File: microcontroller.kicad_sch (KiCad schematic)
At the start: 3 parts, among them J6 JTAG_connector, SW1 SW_Push, U1 STM32G473CBTx

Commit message: Finished schematic and first layout
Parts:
- removed U1: STM32G473CBTx, Package_QFP:LQFP-48_7x7mm_P0.5mm, symbol MCU_ST_STM32G4:STM32G473CBTx
- added C20: 4,7uF, Capacitor_SMD:C_0805_2012Metric, symbol Device:C
- added C21, C22, C23, C24: 100nF, Capacitor_SMD:C_0805_2012Metric, symbol Device:C
- added C25: 1uF, Capacitor_SMD:C_0805_2012Metric, symbol Device:C
- added C26: 10nF, Capacitor_SMD:C_0805_2012Metric, symbol Device:C
- added C28: 0.1uF, Capacitor_SMD:C_0805_2012Metric, symbol Device:C
- added R20: 0, Resistor_SMD:R_0805_2012Metric, symbol Device:R
- added R28: 10k, Resistor_SMD:R_0805_2012Metric, symbol Device:R
- added R29: 1k, Resistor_SMD:R_0805_2012Metric, symbol Device:R
- added U4: STM32F103RGTx, Package_QFP:LQFP-64_10x10mm_P0.5mm, symbol MCU_ST_STM32F1:STM32F103RGTx
- added X1: 831066657, footprints:831066657, symbol my_library:831066657
- J6: footprint (none) -> footprints:627010021621
- SW1: footprint (none) -> footprints:SWT0310
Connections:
- net at SW1.1: now also R29.2
- net +3.3V: now reaches J6.1 (VTref)
- net +3.3V: now also C20.1, C21.1, C22.1, C23.1, C24.1, C25.1, C26.1, R28.1, U4.1 (VBAT), U4.13 (VDDA), U4.19 (VDD), U4.32 (VDD), U4.48 (VDD), U4.64 (VDD), X1.4 (VCC)
- net reset: now reaches J6.10 (~{RESET})
- net reset: now also U4.7 (NRST)
- net swdio: now reaches J6.2 (SWDIO/TMS)
- net swdio: now also U4.46 (PA13)
- net GND: now reaches J6.3 (GND), J6.5 (GND)
- net GND: now also J6.9 (GNDDetect), SW1.3 (2), C20.2, C21.2, C22.2, C23.2, C24.2, C25.2, C26.2, C28.2, R20.1, U4.12 (VSSA), U4.18 (VSS), U4.31 (VSS), U4.47 (VSS), U4.63 (VSS), X1.2 (GND)
- net swclk: now reaches J6.4 (SWCLK/TCK)
- net swclk: now also U4.49 (PA14)
- net swo: now reaches J6.6 (SWO/TDO)
- net swo: now also U4.55 (PB3)
- new net: C28.1, R28.2, R29.1, U4.33 (PB12)
- new net: R20.2, X1.1 (TRI-STATE)
- new net: U4.5 (PD0), X1.3 (OUTPUT)
- new net diaply_cs: U4.20 (PA4)
- new net display_extcomin: U4.24 (PC4)
- new net display_extmode: U4.25 (PC5)
- new net display_mosi: U4.23 (PA7)
- new net display_sck: U4.21 (PA5)
- new net sensor_1_rx: U4.52 (PC11)
- new net sensor_1_tx: U4.51 (PC10)
- new net sensor_2_rx: U4.54 (PD2)
- new net sensor_2_tx: U4.53 (PC12)
- new net usb_dm: U4.44 (PA11)
- new net usb_dp: U4.45 (PA12)
- no-connect marks 0 -> 37
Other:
- note added: "16MHz Oscillator"
- note removed: "32MHz Oscillator"
- title: (none) -> Microcontroller
- moved on the sheet: SW1

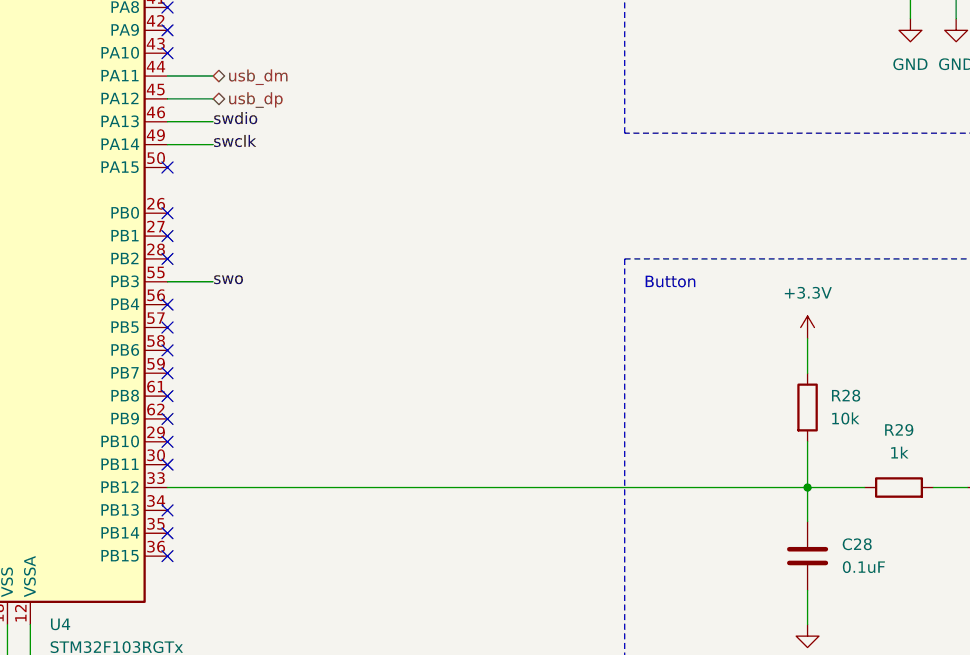
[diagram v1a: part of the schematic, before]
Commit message: Created board outline
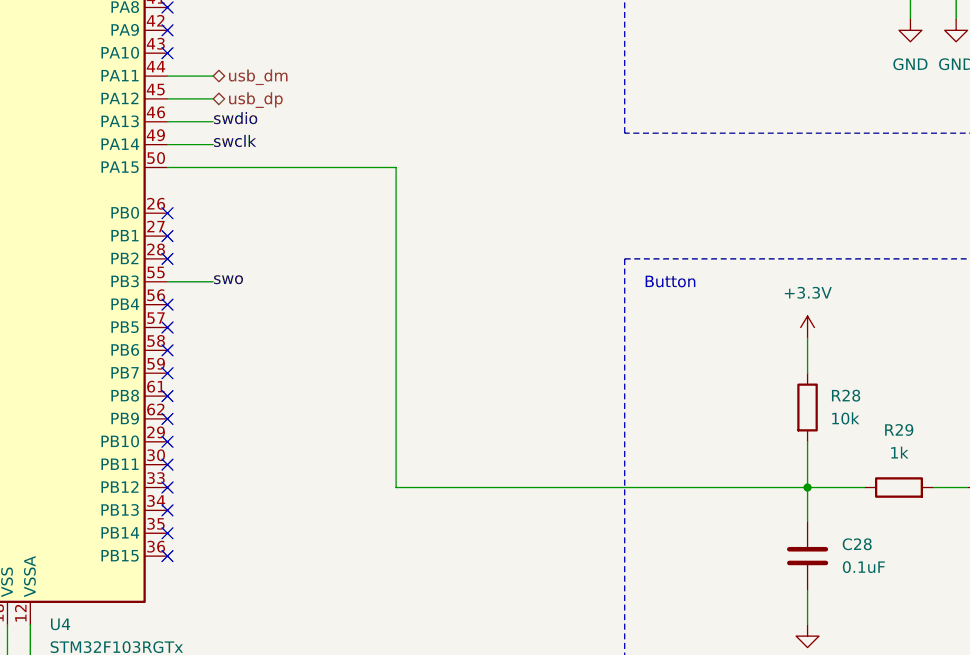
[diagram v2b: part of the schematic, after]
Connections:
- net at C28.1, R28.2, R29.1: now also U4.50 (PA15); no longer U4.33 (PB12)
